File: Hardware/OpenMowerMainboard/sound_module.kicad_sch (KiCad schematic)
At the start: 5 parts, among them J16 Conn_01x08, J23 Conn_01x08

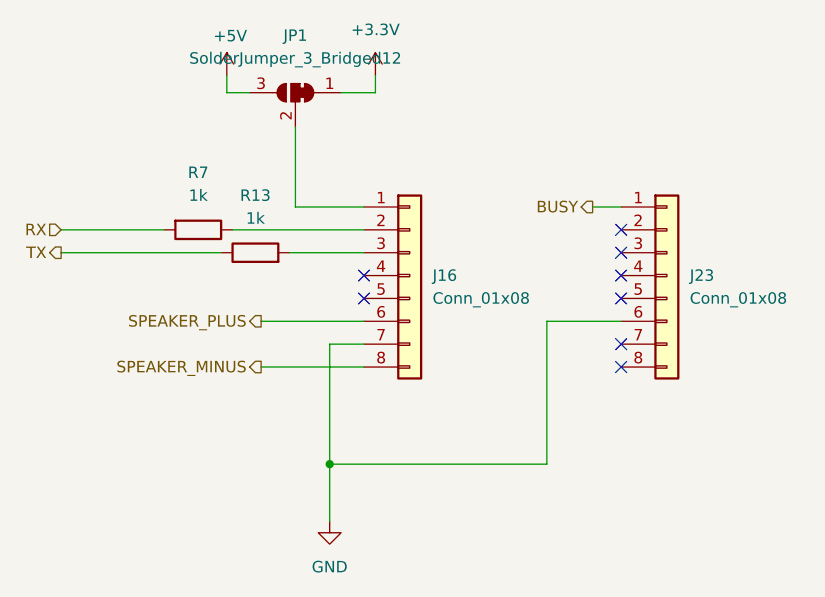
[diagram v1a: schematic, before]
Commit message: feat: update to Kicad7, put back C2,C3
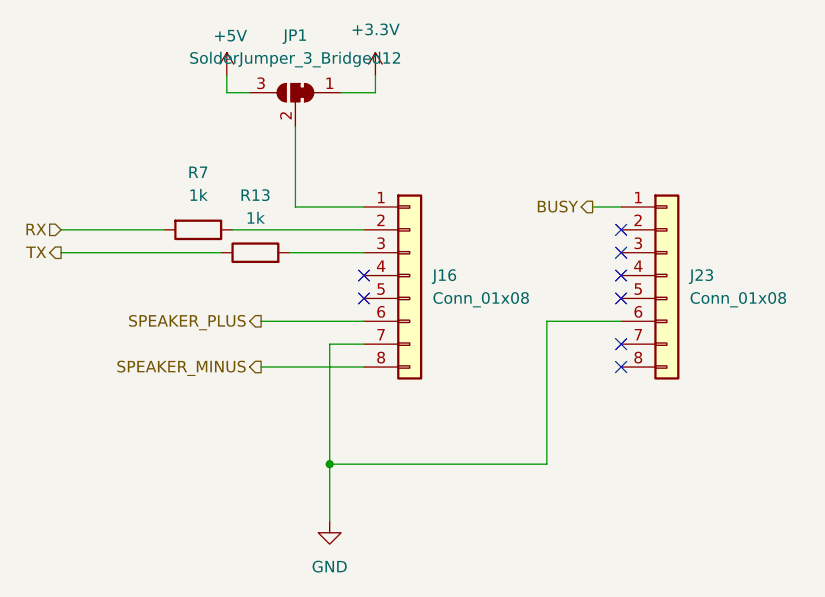
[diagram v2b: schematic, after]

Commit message: feat: remove J4, put back R7,R13 sound resistors
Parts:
- R13, R7: now in the parts list
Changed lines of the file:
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@@
   )
   (symbol (lib_id "Device:R") (at 107.95 134.62 270) (unit 1)
-    (in_bom no) (on_board yes) (dnp no) (fields_autoplaced)
+    (in_bom yes) (on_board yes) (dnp no) (fields_autoplaced)
     (property "Reference" "R7" (at 107.95 128.27 90)
       (effects (font (size 1.27 1.27)))
@@
   )
   (symbol (lib_id "Device:R") (at 114.3 137.16 90) (unit 1)
-    (in_bom no) (on_board yes) (dnp no) (fields_autoplaced)
+    (in_bom yes) (on_board yes) (dnp no) (fields_autoplaced)
     (property "Reference" "R13" (at 114.3 130.81 90)
       (effects (font (size 1.27 1.27)))

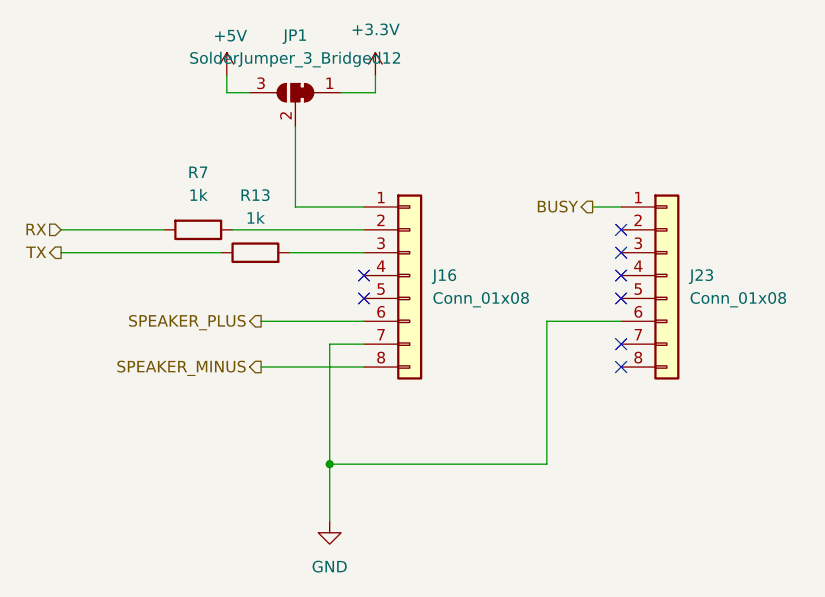
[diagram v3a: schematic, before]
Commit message: upgraded to KiCAD v8
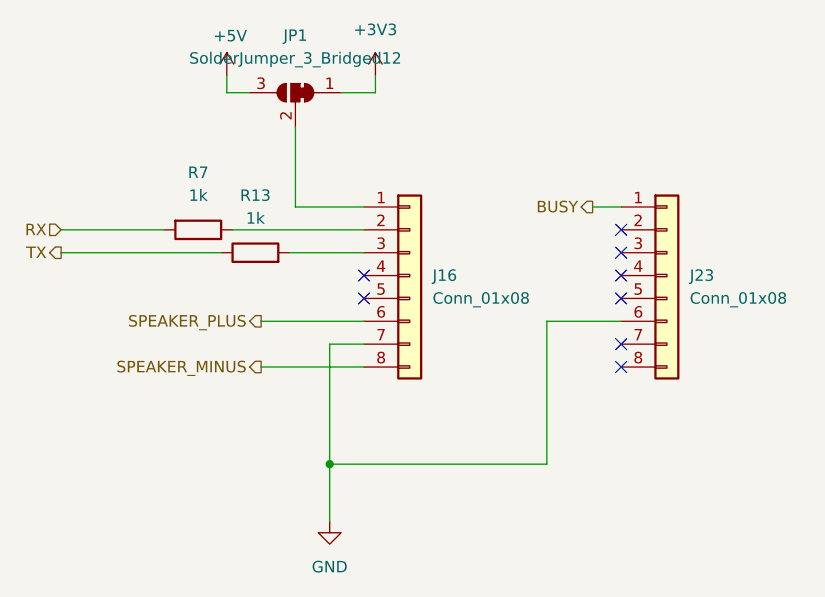
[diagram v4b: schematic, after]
